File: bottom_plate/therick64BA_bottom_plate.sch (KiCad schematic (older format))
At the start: 11 parts, among them U1 HOLE

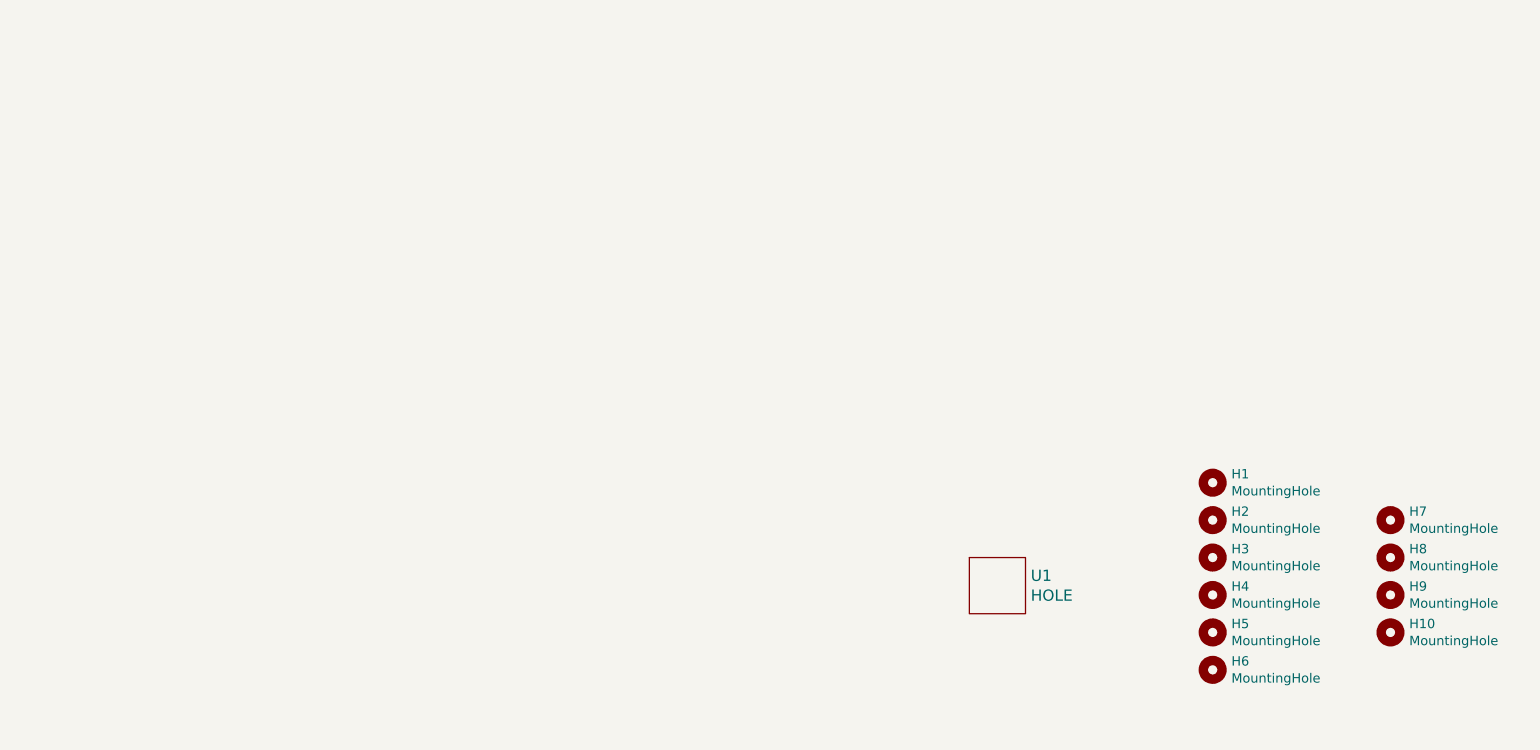
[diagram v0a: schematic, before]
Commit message: Update to 19mm
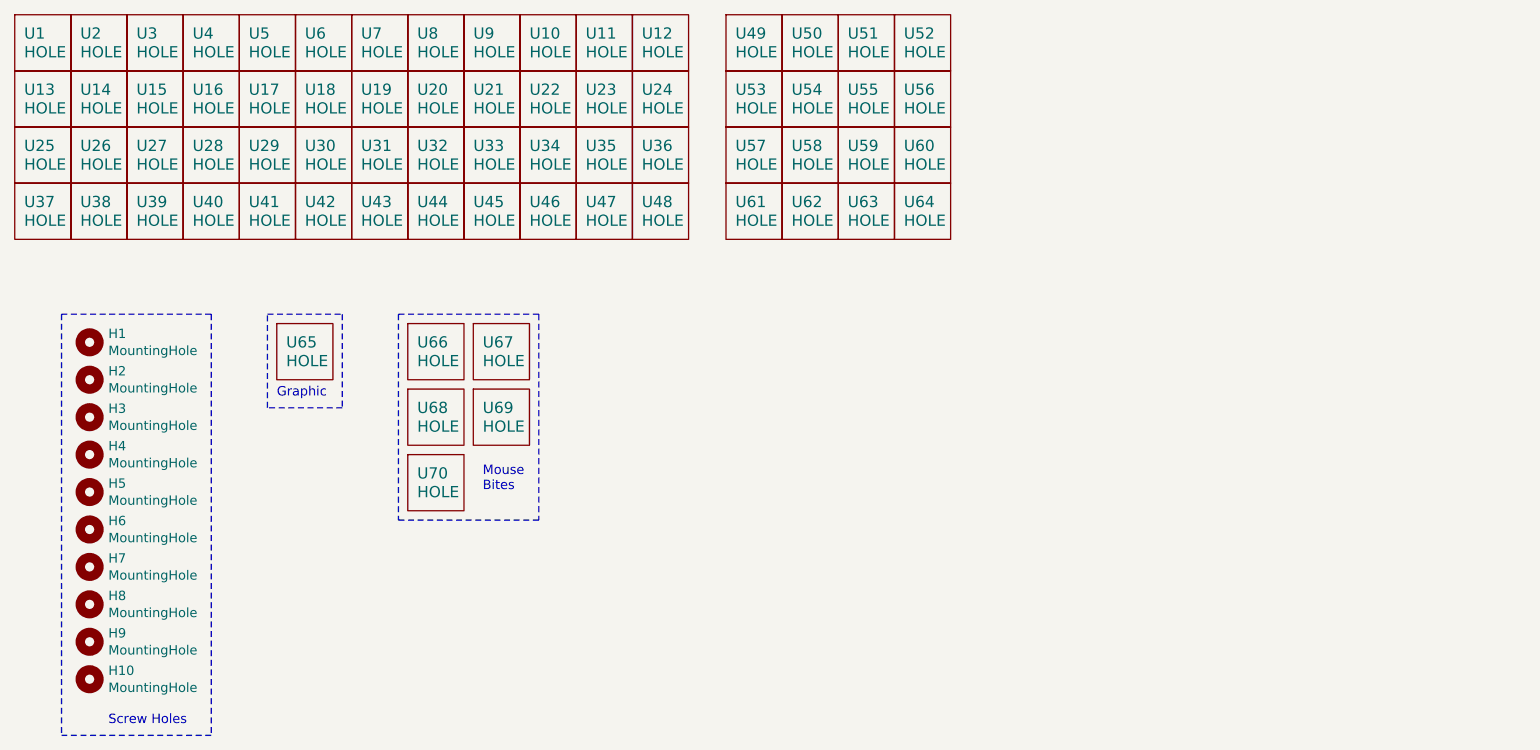
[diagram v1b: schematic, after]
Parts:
- added U10, U11, U12, U13, U14, U15, U16, U17, U18, U19, U2, U20, U21, U22, U23, U24, U25, U26, U27, U28, U29, U3, U30, U31, U32, U33, U34, U35, U36, U37, U38, U39, U4, U40, U41, U42, U43, U44, U45, U46, U47, U48, U49, U5, U50, U51, U52, U53, U54, U55, U56, U57, U58, U59, U6, U60, U61, U62, U63, U64, U7, U8, U9: HOLE, Keeb_footprints:MX100_outline, symbol lets_split-cache:HOLE
- added U65: HOLE, Artwork:rick_large, symbol lets_split-cache:HOLE
- added U66, U67, U68, U69, U70: HOLE, acheron_Hardware:MouseBite_IPC7351, symbol lets_split-cache:HOLE
- U1: footprint Artwork:rick_large -> Keeb_footprints:MX100_outline
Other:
- note added: "Graphic"
- note added: "Mouse\nBites"
- note added: "Screw Holes"
- moved on the sheet: H1, H2, H3, H4, H5, H6
